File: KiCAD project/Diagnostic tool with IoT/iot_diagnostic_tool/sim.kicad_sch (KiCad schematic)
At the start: 11 parts, among them J1 SIM7050-8-0-00-X_REVC

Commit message: Update 06/03/23 - new board layout WIP 70%
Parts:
- removed J1: SIM7050-8-0-00-X_REVC, GCT_SIM7050-8-0-00-X_REVC, symbol SIM7050-8-0-00-X_REVC:SIM7050-8-0-00-X_REVC
- added J3: 693023010811, 693023010811, symbol 693023010811:693023010811
- C32, C33, C34, C35: footprint (none) -> Capacitor_SMD:C_0402_1005Metric
- D5: footprint Package_TO_SOT_SMD_AKL:SOT-363_SC-70-6 -> Package_TO_SOT_SMD:SOT-363_SC-70-6
- R28, R29, R30, R31, R32: footprint (none) -> Resistor_SMD:R_0402_1005Metric
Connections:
- net GND: now also J3.C5 (GND), J3.Z1 (GND1), J3.Z2 (GND1), J3.Z3 (GND1), J3.Z4 (GND1), J3.Z5 (GND1)
- net SIM_DET: now also D5.6 (L5), J3.SW (DETECTION); no longer D5.4 (L3)
- net SIM_RST: now also C33.1, D5.3 (L2), R28.2, J3.C2 (RST)
- net SIM_VDD: now also D5.1 (L1), J3.C1 (VCC); no longer D5.6 (L5)
- net SIM_DAT: now reaches R30.2, R32.2
- net SIM_DAT: now also C35.1, D5.5 (L4), J3.C7 (I/O); no longer C33.1, D5.1 (L1)
- new net SIM_CL: C34.1, D5.4 (L3), J3.C3 (CLK), R29.2
- no-connect marks 1 -> 3
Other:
- moved on the sheet: C32, C33, C34, C35, D5, R28, R29, R30, R31, R32

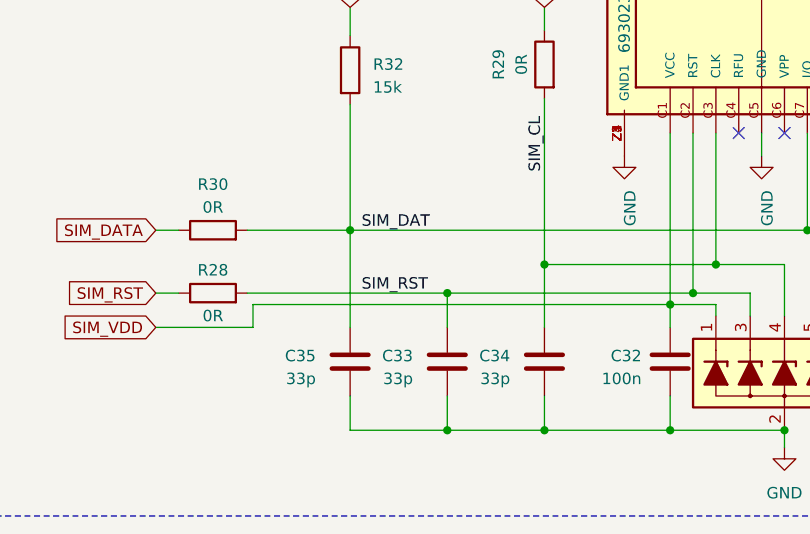
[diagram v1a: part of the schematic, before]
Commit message: Update 13/03/23 - Board layout fixes
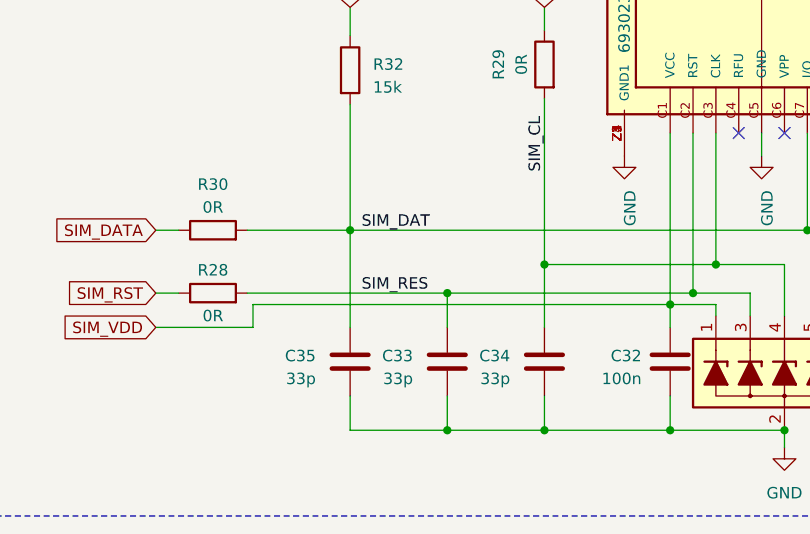
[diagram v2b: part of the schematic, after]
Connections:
- net SIM_RST: no longer C33.1, D5.3 (L2), J3.C2 (RST), R28.2
- new net SIM_RES: C33.1, D5.3 (L2), J3.C2 (RST), R28.2
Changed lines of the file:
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@@
     (effects (font (size 1.27 1.27)) (justify right bottom))
   )
-  (label "SIM_RST" (at 129.54 119.38 0) (fields_autoplaced)
+  (label "SIM_RES" (at 129.54 119.38 0) (fields_autoplaced)
     (effects (font (size 1.27 1.27)) (justify left bottom))
   )

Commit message: Update 17/03/23 - final board update, generated files for manufacturing
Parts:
- C32, C33, C34, C35: footprint Capacitor_SMD:C_0402_1005Metric -> Capacitor_SMD:C_0402_1005Metric_Pad0.74x0.62mm_HandSolder
- D5: footprint Package_TO_SOT_SMD:SOT-363_SC-70-6 -> Package_TO_SOT_SMD:SOT-363_SC-70-6_Handsoldering
- J3: footprint 693023010811 -> 693023010811:693023010811
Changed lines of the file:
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@@
       (effects (font (size 1.27 1.27)) (justify left))
     )
-    (property "Footprint" "Capacitor_SMD:C_0402_1005Metric" (at 138.0998 130.81 0)
+    (property "Footprint" "Capacitor_SMD:C_0402_1005Metric_Pad0.74x0.62mm_HandSolder" (at 138.0998 130.81 0)
       (effects (font (size 1.27 1.27)) hide)
     )
@@
       (effects (font (size 1.27 1.27)) (justify left))
     )
-    (property "Footprint" "Capacitor_SMD:C_0402_1005Metric" (at 127.3048 130.81 0)
+    (property "Footprint" "Capacitor_SMD:C_0402_1005Metric_Pad0.74x0.62mm_HandSolder" (at 127.3048 130.81 0)
       (effects (font (size 1.27 1.27)) hide)
     )
@@
       (effects (font (size 1.27 1.27)) (justify left))
     )
-    (property "Footprint" "Capacitor_SMD:C_0402_1005Metric" (at 162.8648 130.81 0)
+    (property "Footprint" "Capacitor_SMD:C_0402_1005Metric_Pad0.74x0.62mm_HandSolder" (at 162.8648 130.81 0)
       (effects (font (size 1.27 1.27)) hide)
     )
@@
       (effects (font (size 1.27 1.27)) (justify left))
     )
-    (property "Footprint" "693023010811" (at 168.91 91.44 0)
+    (property "Footprint" "693023010811:693023010811" (at 168.91 91.44 0)
       (effects (font (size 1.27 1.27)) (justify bottom) hide)
     )
@@
       (effects (font (size 1.27 1.27)) (justify left))
     )
-    (property "Footprint" "Package_TO_SOT_SMD:SOT-363_SC-70-6" (at 176.53 128.27 0)
+    (property "Footprint" "Package_TO_SOT_SMD:SOT-363_SC-70-6_Handsoldering" (at 176.53 128.27 0)
       (effects (font (size 1.27 1.27)) hide)
     )
@@
       (effects (font (size 1.27 1.27)) (justify left))
     )
-    (property "Footprint" "Capacitor_SMD:C_0402_1005Metric" (at 148.8948 130.81 0)
-      (effects (font (size 1.27 1.27)) hide)
-    )
+    (property "Footprint" "Capacitor_SMD:C_0402_1005Metric_Pad0.74x0.62mm_HandSolder" (at 148.8948 130.81 0)
+      (effects (font (size 1.27 1.27)) hide)
+    )

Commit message: Update 26/06/23 - Thesis release
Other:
- company: (none) -> FEKT VUT
- title: (none) -> OBD Monitoring Device
- moved on the sheet: R32
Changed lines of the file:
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@@
 (kicad_sch (version 20230121) (generator eeschema)
   (paper "A4")
+  (title_block
+    (title "OBD Monitoring Device")
+    (date "2023-02-27")
+    (company "FEKT VUT")
+  )
   (junction (at 139.065 119.38) (diameter 0) (color 0 0 0 0)
   )
@@
     (stroke (width 0) (type default))
   )
-  (wire (pts (xy 128.27 90.805) (xy 128.27 87.63))
+  (wire (pts (xy 128.27 90.17) (xy 128.27 87.63))
     (stroke (width 0) (type default))
   )
@@
     (stroke (width 0) (type default))
   )
-  (wire (pts (xy 128.27 98.425) (xy 128.27 112.395))
+  (wire (pts (xy 128.27 97.79) (xy 128.27 112.395))
     (stroke (width 0) (type default))
   )
@@
   )
   (symbol (lib_id "power:GND") (at 173.99 104.14 0) (unit 1)
-    (in_bom yes) (on_board yes) (dnp no) (fields_autoplaced)
+    (in_bom yes) (on_board yes) (dnp no)
     (property "Reference" "#PWR069" (at 173.99 110.49 0)
       (effects (font (size 1.27 1.27)) hide)
     )
-    (property "Value" "GND" (at 174.625 107.95 90)
+    (property "Value" "GND" (at 175.895 107.95 0)
       (effects (font (size 1.27 1.27)) (justify right))
     )
@@
   (symbol (lib_id "693023010811:693023010811") (at 168.91 91.44 90) (unit 1)
     (in_bom yes) (on_board yes) (dnp no)
-    (property "Reference" "J3" (at 173.5791 75.565 0)
+    (property "Reference" "J3" (at 173.5791 75.565 90)
       (effects (font (size 1.27 1.27)) (justify left))
     )
@@
     )
   )
-  (symbol (lib_id "Device:R") (at 128.27 94.615 0) (unit 1)
+  (symbol (lib_id "Device:R") (at 128.27 93.98 0) (unit 1)
     (in_bom yes) (on_board yes) (dnp no) (fields_autoplaced)
-    (property "Reference" "R32" (at 130.81 93.98 0)
-      (effects (font (size 1.27 1.27)) (justify left))
-    )
-    (property "Value" "15k" (at 130.81 96.52 0)
-      (effects (font (size 1.27 1.27)) (justify left))
-    )
-    (property "Footprint" "Resistor_SMD:R_0402_1005Metric" (at 126.492 94.615 90)
-      (effects (font (size 1.27 1.27)) hide)
-    )
-    (property "Datasheet" "~" (at 128.27 94.615 0)
+    (property "Reference" "R32" (at 130.81 93.345 0)
+      (effects (font (size 1.27 1.27)) (justify left))
+    )
+    (property "Value" "15k" (at 130.81 95.885 0)
+      (effects (font (size 1.27 1.27)) (justify left))
+    )
+    (property "Footprint" "Resistor_SMD:R_0402_1005Metric" (at 126.492 93.98 90)
+      (effects (font (size 1.27 1.27)) hide)
+    )
+    (property "Datasheet" "~" (at 128.27 93.98 0)
       (effects (font (size 1.27 1.27)) hide)
     )
@@
   )
   (symbol (lib_id "power:GND") (at 158.75 104.14 0) (unit 1)
-    (in_bom yes) (on_board yes) (dnp no) (fields_autoplaced)
+    (in_bom yes) (on_board yes) (dnp no)
     (property "Reference" "#PWR045" (at 158.75 110.49 0)
       (effects (font (size 1.27 1.27)) hide)
     )
-    (property "Value" "GND" (at 159.385 107.95 90)
+    (property "Value" "GND" (at 160.655 107.95 0)
       (effects (font (size 1.27 1.27)) (justify right))
     )
@@
   )
   (symbol (lib_id "Device:R") (at 149.86 93.98 0) (mirror y) (unit 1)
-    (in_bom yes) (on_board yes) (dnp no) (fields_autoplaced)
-    (property "Reference" "R29" (at 144.78 93.98 90)
-      (effects (font (size 1.27 1.27)))
-    )
-    (property "Value" "0R" (at 147.32 93.98 90)
-      (effects (font (size 1.27 1.27)))
-    )
+    (in_bom yes) (on_board yes) (dnp no)
+    (property "Reference" "R29" (at 146.05 92.71 0)
+      (effects (font (size 1.27 1.27)))
+    )
+    (property "Value" "0R" (at 146.05 95.25 0)
+      (effects (font (size 1.27 1.27)))
+    )
